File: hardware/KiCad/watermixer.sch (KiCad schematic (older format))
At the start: 15 parts, among them U1 Display, U2 ESP32-DevKitC, U3 LLC_4CH, U4 MCP4728

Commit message: Pcb parts placed, but no traces yet
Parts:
- added C2, C3: 470uF, Capacitor_THT:CP_Radial_Tantal_D8.0mm_P5.00mm, symbol watermixer-symbols:CP
- added H1, H2, H3, H4: MountingHole, watermixer-footprints:MountingHole_3.2mm_M3, symbol watermixer-symbols:MountingHole
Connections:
- net GND: now also C2.2, C3.2
- net VCC: now also C3.1
- net VDDF: now also C2.1
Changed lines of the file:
@@
 $EndDescr
-$Comp
-L watermixer-symbols:MCP4728 U4
-U 1 1 613FB3CB
-P 8700 5200
-F 0 "U4" H 8500 5450 50  0000 C CNN
-F 1 "MCP4728" H 8950 5450 50  0000 C CNN
-F 2 "watermixer-footprints:MCP4728_module" H 8700 4600 50  0001 C CNN
-F 3 "http://ww1.microchip.com/downloads/en/DeviceDoc/22187E.pdf" H 8700 5450 50  0001 C CNN
-	1    8700 5200
-	1    0    0    -1
-$EndComp
 $Comp
 L Espressif:ESP32-DevKitC U2
@@
 Wire Wire Line
 	6800 1150 8700 1150
-Wire Wire Line
-	8700 1150 8700 4850
 Connection ~ 8700 4850
 Wire Wire Line
@@
 Wire Wire Line
 	5250 7150 5550 7150
-Wire Wire Line
-	5550 7150 5550 7000
 $Comp
 L power:GND #PWR08
@@
 	4300 3950 4650 3950
 Wire Wire Line
-	4300 3950 4300 5250
+	4300 3950 4300 4900
 Wire Wire Line
 	4300 3350 4300 3500
@@
 Connection ~ 8450 2950
 Wire Wire Line
-	5750 7000 5550 7000
+	5750 7000 5700 7000
 Connection ~ 5550 7000
 Wire Wire Line
 	2650 4100 2650 4250
 Wire Wire Line
-	5550 7550 5750 7550
+	5550 7550 5700 7550
 Connection ~ 5550 7550
 NoConn ~ 3000 2950
@@
 $EndComp
 Wire Wire Line
-	4750 4850 4750 5100
+	4750 4850 4750 4900
 Wire Wire Line
 	5500 5100 5100 5100
@@
 Wire Wire Line
 	4750 5100 4750 5250
+Wire Wire Line
+	8700 1150 8700 4850
+$Comp
+L watermixer-symbols:CP C2
+U 1 1 6148D5D9
+P 4550 4900
+F 0 "C2" V 4450 4800 50  0000 C CNN
+F 1 "470uF" V 4700 4900 50  0000 C CNN
+F 2 "Capacitor_THT:CP_Radial_Tantal_D8.0mm_P5.00mm" H 4550 4500 50  0001 C CNN
+F 3 "~" H 4550 4900 50  0001 C CNN
+	1    4550 4900
+	0    1    1    0
+$EndComp
+Wire Wire Line
+	4400 4900 4300 4900
+Connection ~ 4300 4900
+Wire Wire Line
+	4300 4900 4300 5250
+Wire Wire Line
+	4700 4900 4750 4900
+Connection ~ 4750 4900
+Wire Wire Line
+	4750 4900 4750 5100
+$Comp
+L watermixer-symbols:CP C3
+U 1 1 6149C94A
+P 5700 7250
+F 0 "C3" V 5600 7150 50  0000 C CNN
+F 1 "470uF" V 5850 7250 50  0000 C CNN
+F 2 "Capacitor_THT:CP_Radial_Tantal_D8.0mm_P5.00mm" H 5700 6850 50  0001 C CNN
+F 3 "~" H 5700 7250 50  0001 C CNN
+	1    5700 7250
+	1    0    0    -1
+$EndComp
+Wire Wire Line
+	5550 7000 5550 7150
+Wire Wire Line
+	5700 7100 5700 7000
+Connection ~ 5700 7000
+Wire Wire Line
+	5700 7000 5550 7000
+Wire Wire Line
+	5700 7400 5700 7550
+Connection ~ 5700 7550
+Wire Wire Line
+	5700 7550 5750 7550
+$Comp
+L watermixer-symbols:MCP4728 U4
+U 1 1 614D13D0
+P 8700 5200
+F 0 "U4" H 8700 5681 50  0000 C CNN
+F 1 "MCP4728" H 8700 5590 50  0000 C CNN
+F 2 "watermixer-footprints:MCP4728_module" H 8700 4600 50  0001 C CNN
+F 3 "http://ww1.microchip.com/downloads/en/DeviceDoc/22187E.pdf" H 8700 5450 50  0001 C CNN
+	1    8700 5200
+	1    0    0    -1
+$EndComp
+$Comp
+L watermixer-symbols:MountingHole H4
+U 1 1 614E9C53
+P 700 7450
+F 0 "H4" H 800 7496 50  0000 L CNN
+F 1 "MountingHole" H 800 7405 50  0000 L CNN
+F 2 "watermixer-footprints:MountingHole_3.2mm_M3" H 700 7450 50  0001 C CNN
+F 3 "~" H 700 7450 50  0001 C CNN
+	1    700  7450
+	1    0    0    -1
+$EndComp
+$Comp
+L watermixer-symbols:MountingHole H3
+U 1 1 614EA463
+P 700 7250
+F 0 "H3" H 800 7296 50  0000 L CNN
+F 1 "MountingHole" H 800 7205 50  0000 L CNN
+F 2 "watermixer-footprints:MountingHole_3.2mm_M3" H 700 7250 50  0001 C CNN
+F 3 "~" H 700 7250 50  0001 C CNN
+	1    700  7250
+	1    0    0    -1
+$EndComp
+$Comp
+L watermixer-symbols:MountingHole H2
+U 1 1 614EAA78
+P 700 7050
+F 0 "H2" H 800 7096 50  0000 L CNN
+F 1 "MountingHole" H 800 7005 50  0000 L CNN
+F 2 "watermixer-footprints:MountingHole_3.2mm_M3" H 700 7050 50  0001 C CNN
+F 3 "~" H 700 7050 50  0001 C CNN
+	1    700  7050
+	1    0    0    -1
+$EndComp
+$Comp
+L watermixer-symbols:MountingHole H1
+U 1 1 614EB1BF
+P 700 6850
+F 0 "H1" H 800 6896 50  0000 L CNN
+F 1 "MountingHole" H 800 6805 50  0000 L CNN
+F 2 "watermixer-footprints:MountingHole_3.2mm_M3" H 700 6850 50  0001 C CNN
+F 3 "~" H 700 6850 50  0001 C CNN
+	1    700  6850
+	1    0    0    -1
+$EndComp
 $EndSCHEMATC

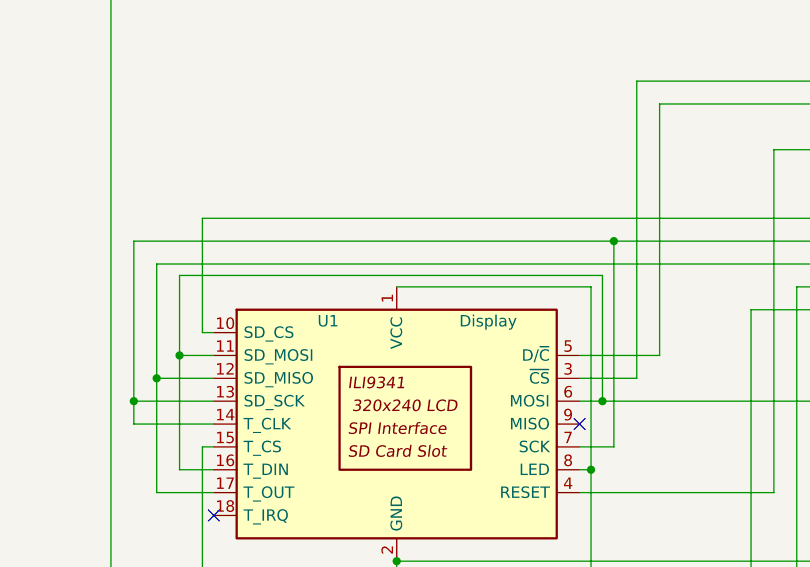
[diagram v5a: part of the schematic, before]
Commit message: Connected all on PCB except GND
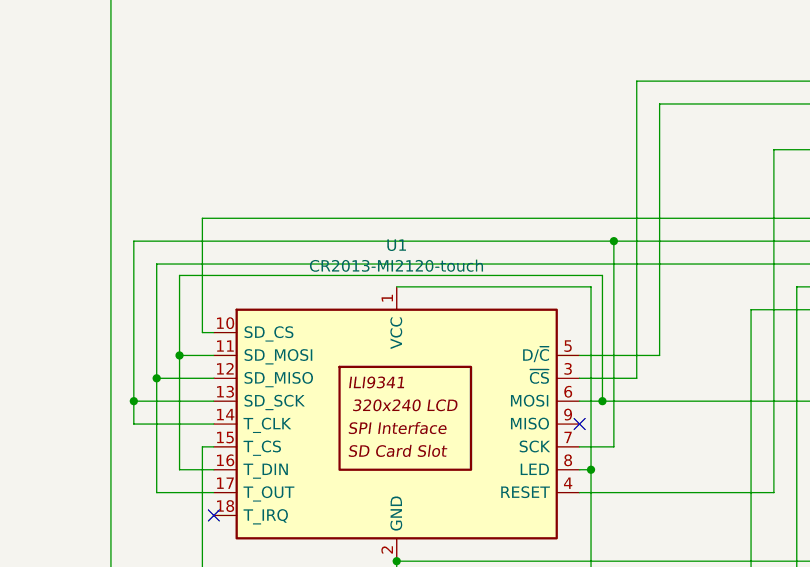
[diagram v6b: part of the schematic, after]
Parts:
- U1: value Display -> CR2013-MI2120-touch
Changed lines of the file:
@@
 	0    1    1    0
-$EndComp
-$Comp
-L watermixer-symbols:CR2013-MI2120-touch U1
-U 1 1 6143BF69
-P 2200 2950
-F 0 "U1" H 1900 3400 50  0000 C CNN
-F 1 "Display" H 2600 3400 50  0000 C CNN
-F 2 "watermixer-footprints:CR2013-MI2120_touch" H 2200 2250 50  0001 C CNN
-F 3 "http://pan.baidu.com/s/11Y990" H 1550 3450 50  0001 C CNN
-	1    2200 2950
-	1    0    0    -1
 $EndComp
 Wire Wire Line
@@
 Wire Wire Line
 	4050 3550 4050 2950
-Connection ~ 2200 3550
 Wire Wire Line
 	4900 4850 8450 4850
@@
 	1    0    0    -1
 $EndComp
+$Comp
+L watermixer-symbols:CR2013-MI2120-touch U1
+U 1 1 6142F819
+P 2200 2950
+F 0 "U1" H 2200 3731 50  0000 C CNN
+F 1 "CR2013-MI2120-touch" H 2200 3640 50  0000 C CNN
+F 2 "watermixer-footprints:CR2013-MI2120_touch" H 2200 2250 50  0001 C CNN
+F 3 "http://pan.baidu.com/s/11Y990" H 1550 3450 50  0001 C CNN
+	1    2200 2950
+	1    0    0    -1
+$EndComp
+Connection ~ 2200 3550
 $EndSCHEMATC

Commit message: added ADS1115 to pcb and ordered 5 pcbs with current production
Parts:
- removed R2: 4.7k, Resistor_THT:R_Axial_DIN0207_L6.3mm_D2.5mm_P7.62mm_Horizontal, symbol watermixer-symbols:R
- removed R3: 3.3k, Resistor_THT:R_Axial_DIN0207_L6.3mm_D2.5mm_P7.62mm_Horizontal, symbol watermixer-symbols:R
- removed U4: MCP4728, watermixer-footprints:MCP4728_module, symbol watermixer-symbols:MCP4728
- removed U_3.3V1, U_5V1: SD_BUCK3A, watermixer-footprints:SD_BUCK3A, symbol watermixer-symbols:SD_BUCK3A
- added U4: MCP4728, watermixer-footprints:MCP4728_module, symbol watermixer-rescue:MCP4728-watermixer-symbols-watermixer-rescue
- added U5: ADS1115, watermixer-footprints:ADS1115_module, symbol watermixer-symbols:ADS1115
- added U6, U7: SD_BUCK3A, watermixer-footprints:SD_BUCK3A, symbol watermixer-symbols:SD_BUCK3A
- U2: symbol Espressif:ESP32-DevKitC -> watermixer-symbols:ESP32-DevKitC
- U3: symbol watermixer-symbols:LLC_4CH -> watermixer-rescue:LLC_4CH-watermixer-symbols-watermixer-rescue
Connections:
- net GND: now also U4.10 (GND), U5.10 (GND), U6.3 (GND_IN), U6.4 (GND_OUT), U6.7 (GND_IN), U6.8 (GND_OUT), U7.3 (GND_IN), U7.4 (GND_OUT), U7.7 (GND_IN), U7.8 (GND_OUT)
- net at U3.11 (HV4): now also U4.3 (SDA), U5.3 (SDA)
- net at U3.9 (HV3): now also U4.2 (SCL), U5.2 (SCL)
- net at JHC_VALVES1.3: now also U4.6 (VOUTA)
- net at JHC_VALVES1.6: now also U4.7 (VOUTB)
- net at JD_VALVE1.3: now also U4.9 (VOUTD)
- net SIG renamed SIGT
- net SIGT: no longer JPress1.3
- net VCC renamed +12V
- net +12V: now also U6.1 (IN_VCC), U6.5 (IN_VCC), U7.1 (IN_VCC), U7.5 (IN_VCC)
- net VDD renamed +3V3
- net +3V3: now also U7.2 (VCC_OUT), U7.6 (VCC_OUT)
- net VDDF renamed +5V
- net +5V: now also U4.1 (VDD), U5.1 (VDD), U6.2 (VCC_OUT), U6.6 (VCC_OUT)
- new net SIGP: JPress1.3, U5.6 (A0)
- no-connect marks 30 -> 36
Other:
- moved on the sheet: C1, C2, C3, H1, H2, H3, H4, JPress1, J_12V1, R1
